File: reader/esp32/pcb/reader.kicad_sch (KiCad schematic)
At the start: 29 parts, among them J2 RS485, J4 Debug, Q1 MMBT3904, Q2 MMBT3904, U1 ESP32-WROOM-32U, U3 MAX485E, U5 AMS1117-3.3, U5 RDM6300

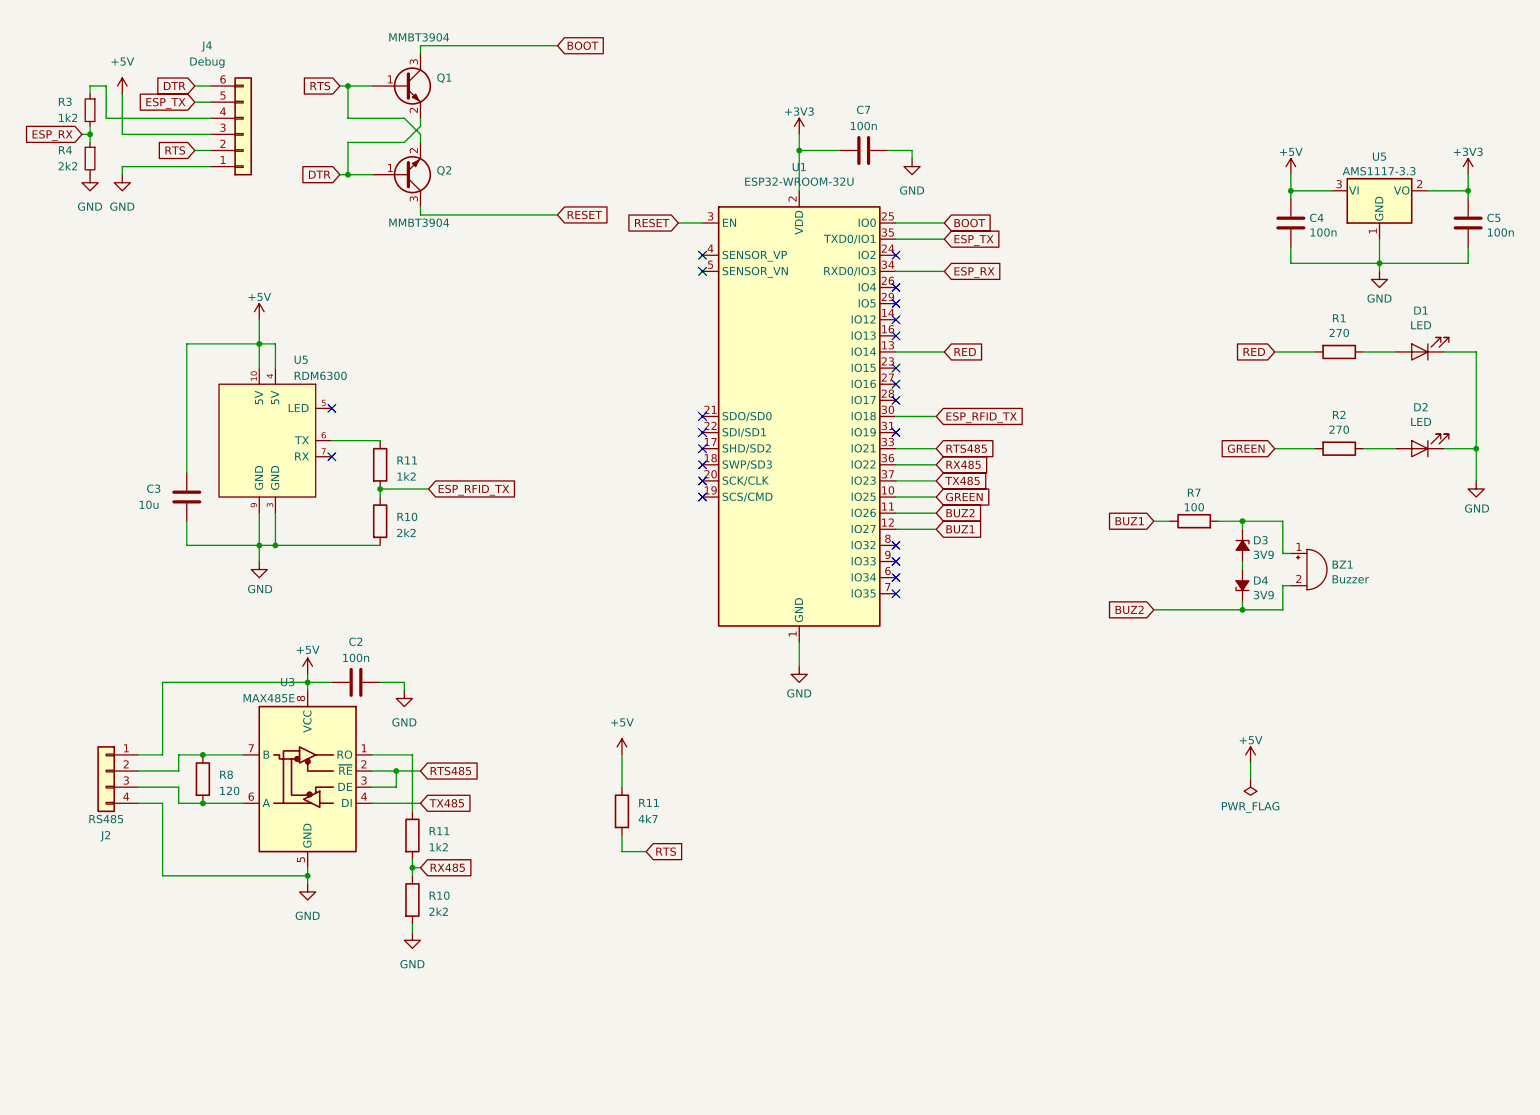
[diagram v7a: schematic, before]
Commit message: Add reset/boot switches, minimize size.
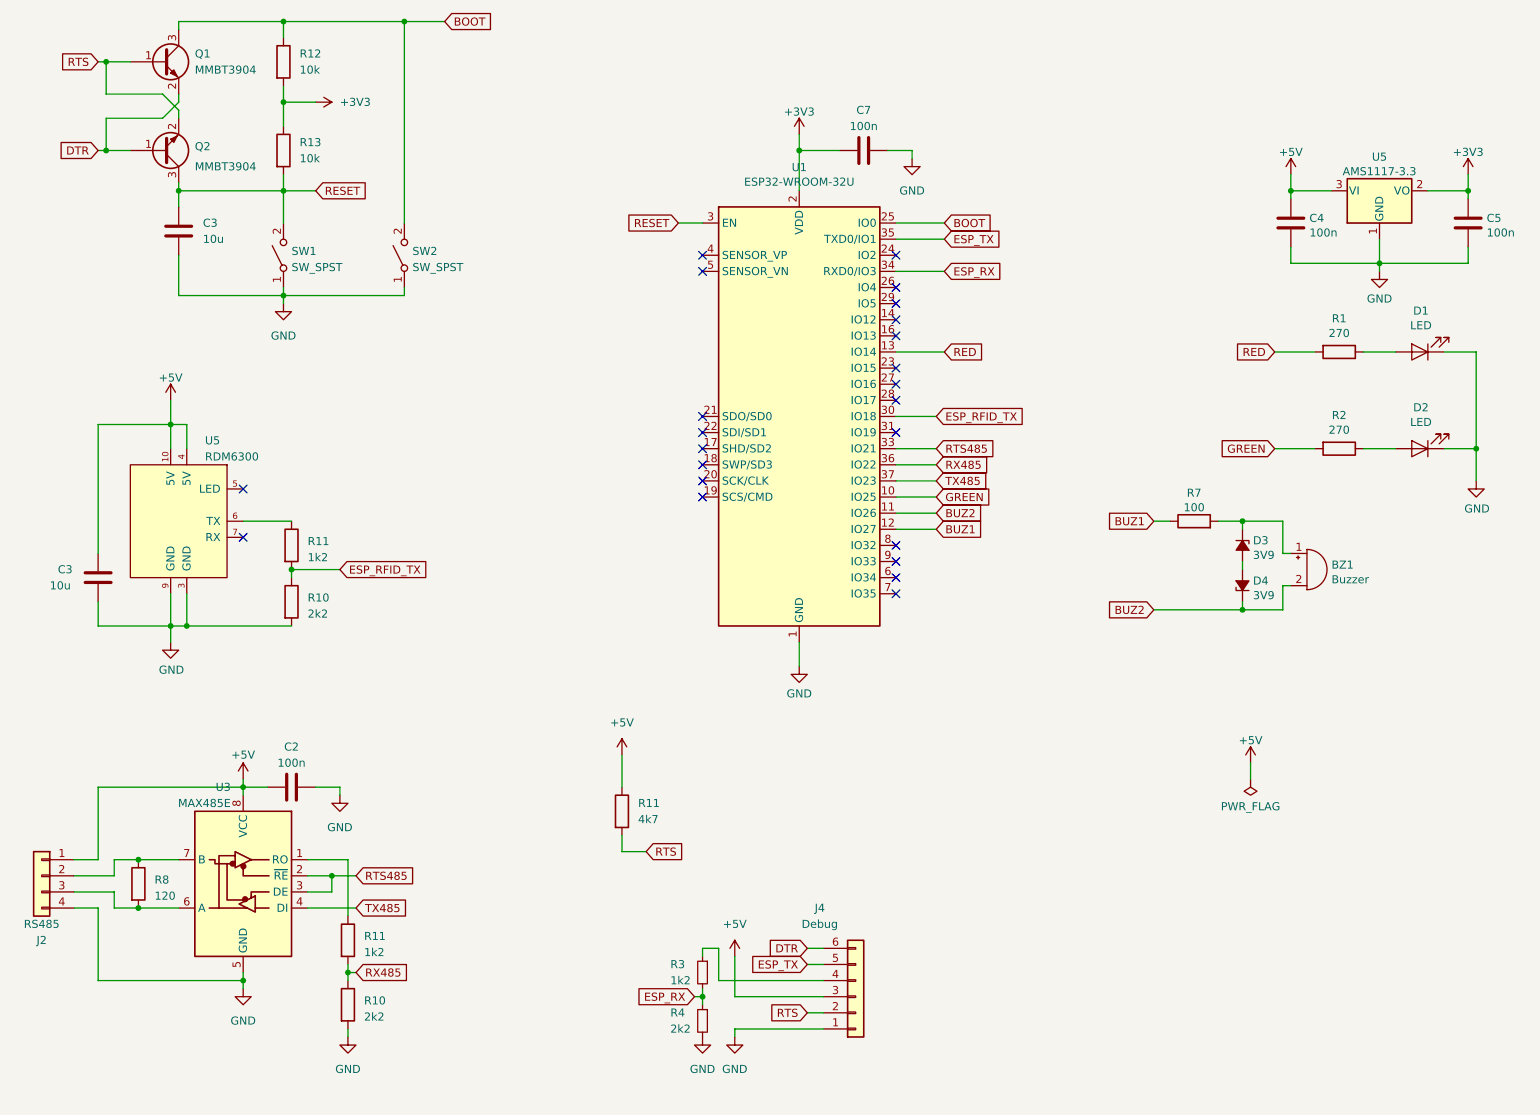
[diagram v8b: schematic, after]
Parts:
- added C3: 10u, Capacitor_SMD:C_0805_2012Metric, symbol Device:C
- added R12, R13: 10k, Resistor_SMD:R_0603_1608Metric, symbol Device:R
- added SW1, SW2: SW_SPST, Button_Switch_SMD:SW_SPST_CK_RS282G05A3, symbol Switch:SW_SPST
- C3: footprint Capacitor_SMD:C_0603_1608Metric -> Capacitor_SMD:C_0805_2012Metric
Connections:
- net +3V3: now also R12.2, R13.1
- net BOOT: now also R12.1, SW2.2 (B)
- net GND: now also C3.2, SW1.1 (A), SW2.1 (A)
- net RESET: now also C3.1, R13.2, SW1.2 (B)
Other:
- moved on the sheet: C2, C3, J2, J4, R10, R11, R3, R4, R8, U3, U5
